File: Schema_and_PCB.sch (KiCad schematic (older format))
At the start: 0 parts

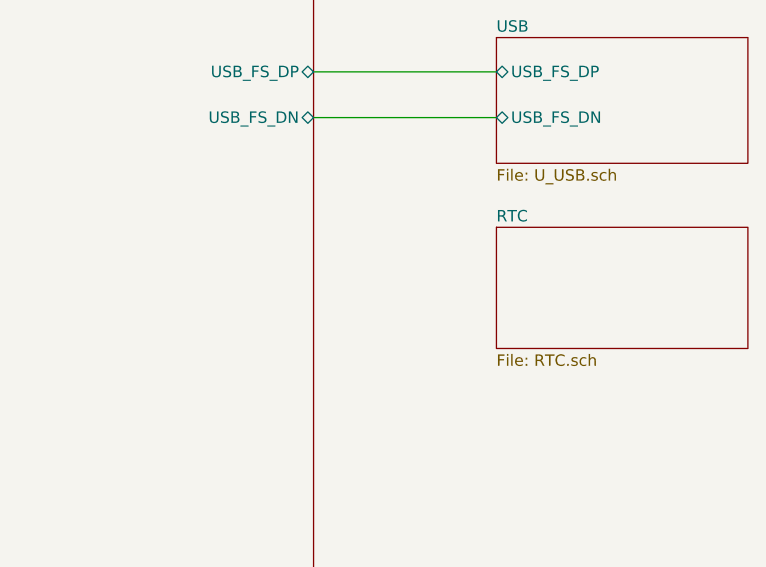
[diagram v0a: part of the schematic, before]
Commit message: RTC DS3231 layot finished
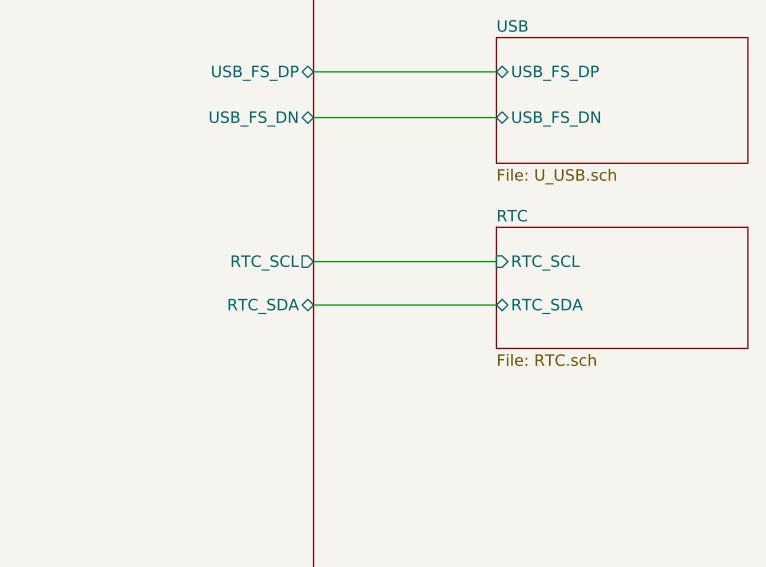
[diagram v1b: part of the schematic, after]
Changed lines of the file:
@@
 F51 "SPI1_SCK" O R 7750 2400 50
 F52 "SPI1_MOSI" O R 7750 2250 50
+F53 "RTC_SCL" O R 7750 4330 50
+F54 "RTC_SDA" B R 7750 4520 50
 $EndSheet
 Wire Wire Line
@@
 F0 "RTC" 50
 F1 "RTC.sch" 50
+F2 "RTC_SCL" I L 8550 4330 50
+F3 "RTC_SDA" B L 8550 4520 50
 $EndSheet
+Wire Wire Line
+	7750 4330 8550 4330
+Wire Wire Line
+	8550 4520 7750 4520
 $EndSCHEMATC
